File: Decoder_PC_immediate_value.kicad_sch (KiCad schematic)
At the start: 0 parts

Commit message: Added storage flash
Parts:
- added U1: ~, Package_LCC:PLCC-32_11.4x14.0mm_P1.27mm, symbol Other:SST39SF010A-55-4C
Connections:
- new net AUX_1: U1.12 (A0)
- new net OP_Code_1: U1.6 (A6)
- new net OP_Code_2: U1.5 (A7)
- new net OP_Code_3: U1.27 (A8)
- new net OP_Code_4: U1.26 (A9)
- new net OP_Code_5: U1.23 (A10)
- new net OP_Code_6: U1.25 (A11)
- new net OP_Code_7: U1.4 (A12)
- new net OP_Code_8: U1.28 (A13)
- new net OP_Code_9: U1.29 (A14)
- new net PM: U1.2 (A16)
- new net Stage_1: U1.11 (A1)
- new net Stage_2: U1.10 (A2)
- new net Stage_3: U1.9 (A3)
- new net Stage_4: U1.8 (A4)
- new net Stage_5: U1.7 (A5)
- new net ZF: U1.3 (A15)

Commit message: Added /WE
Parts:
- added C1: 0.1µF, Capacitor_SMD:C_0805_2012Metric_Pad1.18x1.45mm_HandSolder, symbol Device:C_Small
- added R1: 330Ω, Resistor_SMD:R_0805_2012Metric_Pad1.20x1.40mm_HandSolder, symbol Device:R
- added TP1: /WE, TestPoint:TestPoint_Pad_D1.0mm, symbol Connector:TestPoint
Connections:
- net ControlWord0: now reaches U1.13 (DQ0)
- net ControlWord1: now reaches U1.14 (DQ1)
- net ControlWord2: now reaches U1.15 (DQ2)
- net GND: now reaches U1.16 (Vss)
- net GND: now also C1.1
- net ControlWord3: now reaches U1.17 (DQ3)
- net ControlWord4: now reaches U1.18 (DQ4)
- net ControlWord5: now reaches U1.19 (DQ5)
- net ControlWord6: now reaches U1.20 (DQ6)
- net ControlWord7: now reaches U1.21 (DQ7)
- net /CE: now reaches U1.22 (CE#)
- net /OE: now reaches U1.24 (OE#)
- net /WE: now reaches U1.31 (WE#)
- net /WE: now also R1.1, TP1.1
- net VCC: now reaches U1.32 (Vdd)
- net VCC: now also C1.2, R1.2

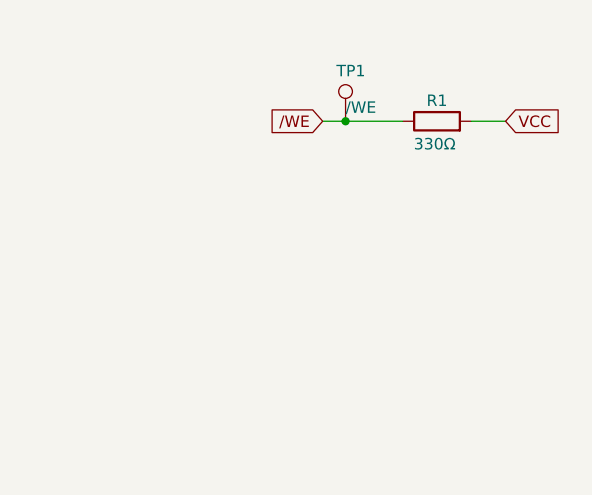
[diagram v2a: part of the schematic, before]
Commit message: Added default pulls for /WE, /CE & /OE
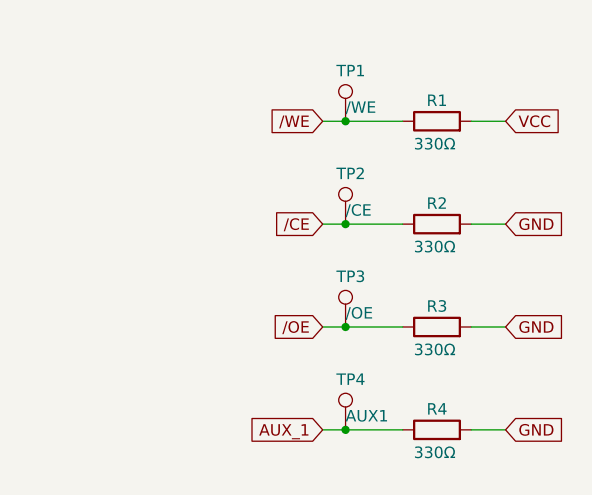
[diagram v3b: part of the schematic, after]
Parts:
- added R2, R3, R4: 330Ω, Resistor_SMD:R_0805_2012Metric_Pad1.20x1.40mm_HandSolder, symbol Device:R
- added TP2: /CE, TestPoint:TestPoint_Pad_D1.0mm, symbol Connector:TestPoint
- added TP3: /OE, TestPoint:TestPoint_Pad_D1.0mm, symbol Connector:TestPoint
- added TP4: AUX1, TestPoint:TestPoint_Pad_D1.0mm, symbol Connector:TestPoint
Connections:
- net AUX_1: now also R4.1, TP4.1
- net GND: now also R2.2, R3.2, R4.2
- net /CE: now also R2.1, TP2.1
- net /OE: now also R3.1, TP3.1
